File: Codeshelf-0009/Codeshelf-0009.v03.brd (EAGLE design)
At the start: 55.8 x 40.9 mm, 28 parts, among them J1 CONTACT-SPRING-S7071-42R, J2 CONTACT-SPRING-S7071-42R, J3 CONTACT-SPRING-S7071-42R, J4 CONTACT-SPRING-S7071-42R, U1 MC9S08QG-DT, U2 LED5060A, U3 RS485SOIC, U4 CAT9552

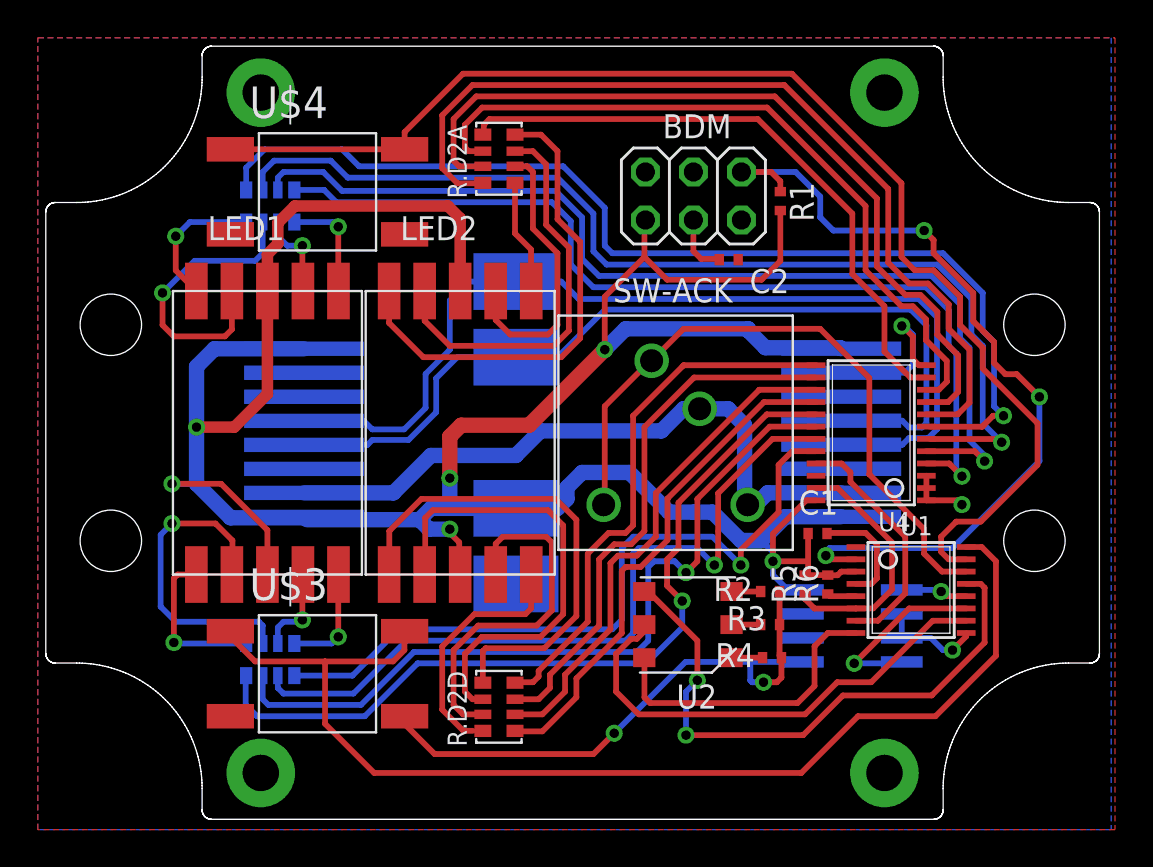
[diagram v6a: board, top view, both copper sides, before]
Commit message: New PosCon CAD model + routing
Added latest CAD model (sent to Marc) and did a little bit of routing.
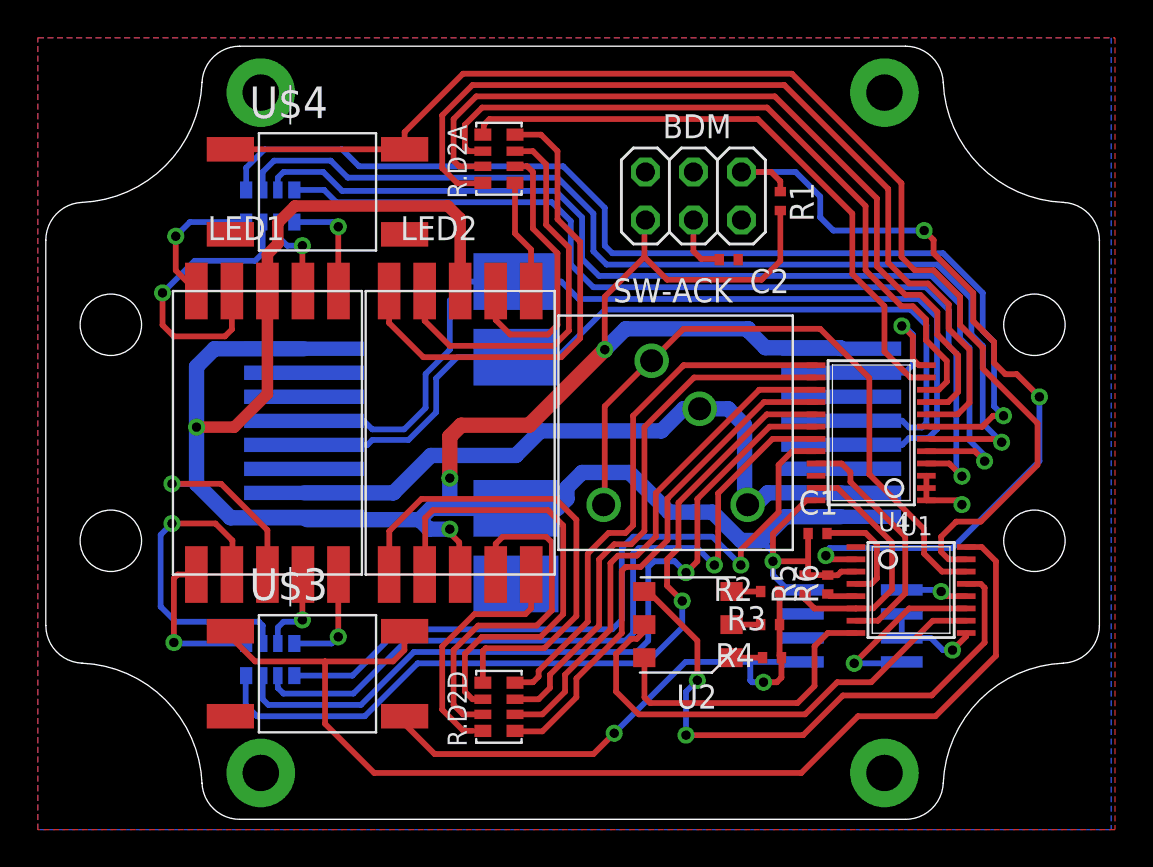
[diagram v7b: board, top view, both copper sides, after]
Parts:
- turned J2 to 270 degrees
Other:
- outline, holes or cut-outs redrawn

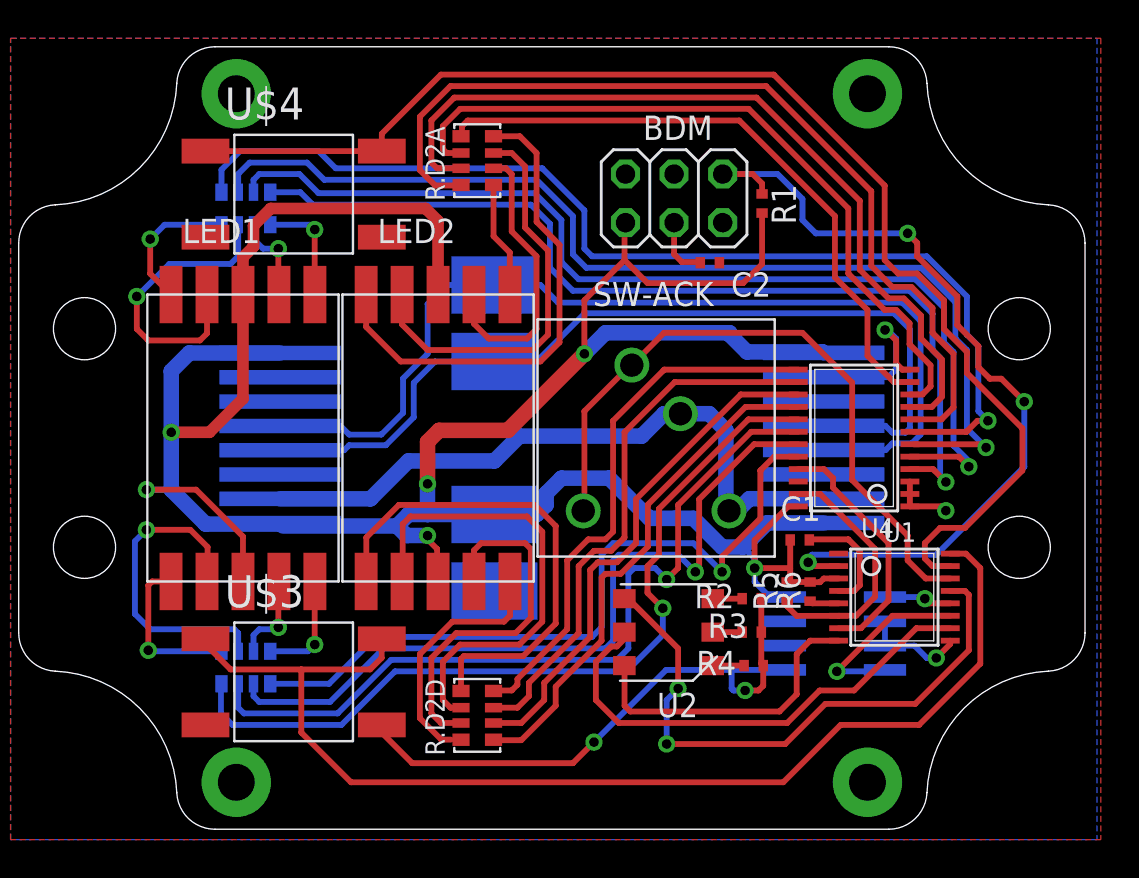
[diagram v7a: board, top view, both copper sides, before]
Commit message: New PosCon finished routing
Added RJ45 programming and awaiting new LED test.
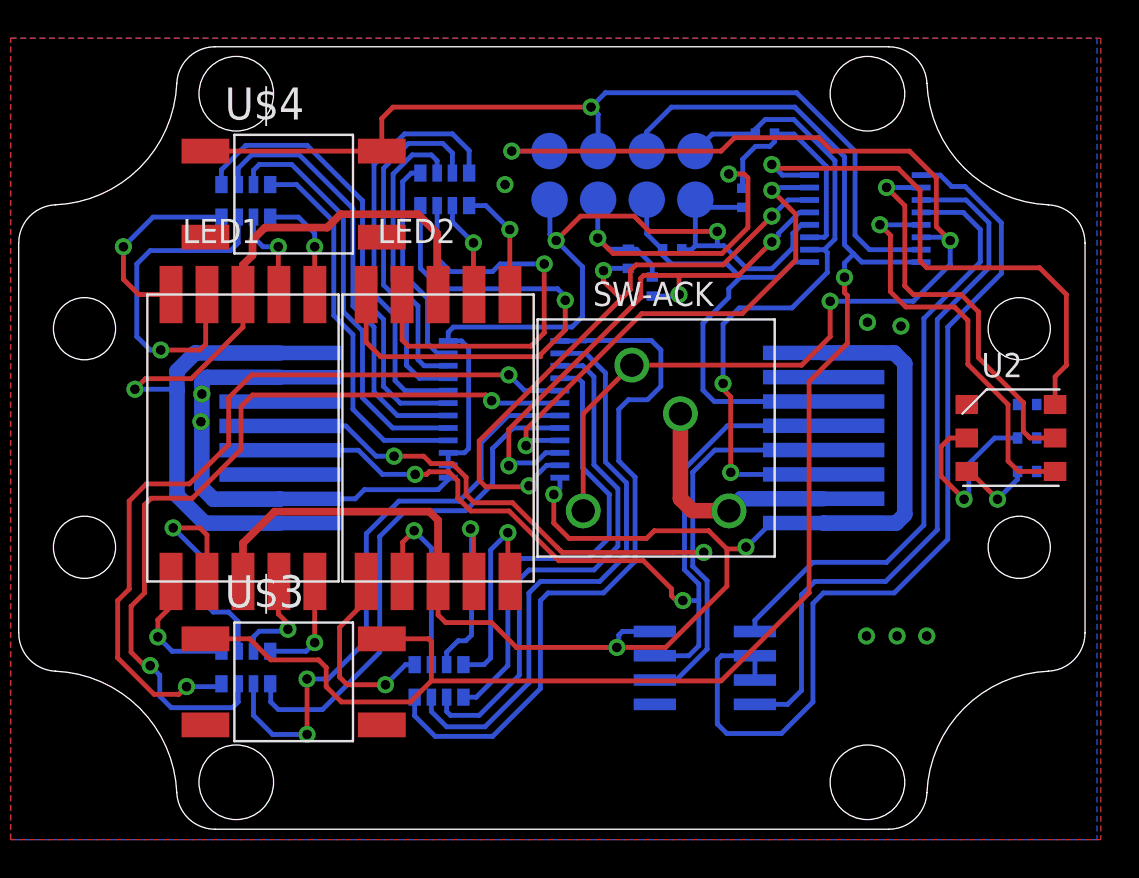
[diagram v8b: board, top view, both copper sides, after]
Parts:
- removed J1, J2, J3, J4: CONTACT-SPRING-S7071-42R, GW-devices:CONTACT-SPRING-S1761
- BDM: value HEADER-3X2 -> TP2X4SMD; device GW-devices:HEADER-3X2 -> GW-devices:SMD4X2
- moved U2 20.6 mm to (24.0, 0.00), turned to 0 degrees
- moved U1 19.8 mm to (16.4, 11.5), flipped to the bottom, turned to 90 degrees
- moved R4 19.8 mm to (24.9, 1.75), flipped to the bottom, turned to 180 degrees
- moved R5 19.3 mm to (4.00, 9.37), flipped to the bottom
- moved U4 18.4 mm to (-2.50, 1.50), flipped to the bottom
- moved C1 18.1 mm to (9.98, 12.6), flipped to the bottom, turned to 270 degrees
- moved R6 18.0 mm to (5.25, 7.92), flipped to the bottom
- moved R3 17.6 mm to (24.9, 0.00), flipped to the bottom, turned to 180 degrees
- moved R2 15.9 mm to (24.9, -1.75), flipped to the bottom, turned to 180 degrees
- moved U3 7.03 mm to (8.00, -12.0)
- moved BDM 3.84 mm to (7.50, 15.0), flipped to the bottom, turned to 0 degrees
- moved R1 3.63 mm to (11.1, 15.9), flipped to the bottom, turned to 180 degrees
- moved R.D2D 2.69 mm to (-5.90, -12.7), flipped to the bottom, turned to 0 degrees
- moved R.D2A 2.27 mm to (-5.60, 13.0), flipped to the bottom, turned to 0 degrees
- moved C2 2.08 mm to (6.29, 9.84), flipped to the bottom, turned to 0 degrees
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- renumbered U$2 to U$2-PROG
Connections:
- net +3V3: now also BDM.P$6; no longer BDM.6, J1.P1
- net 485_N: no longer J2.P1
- net 485_P: no longer J3.P1
- net GND: now also BDM.P$2, BDM.P$8; no longer BDM.2, J4.P1
- net N$23: now also BDM.P$4, U$1.P$3; no longer BDM.4
- net N$42: now also BDM.P$7
- net N$43: now also BDM.P$5
- net N$45: now also BDM.P$3
- net N$9: now also BDM.P$1, U$1.P$6; no longer BDM.1
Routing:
- net N$19: track 5.43 -> 49.1 mm, vias 1 -> 0
- net N$13: track 55.3 -> 22.7 mm, vias 1 -> 0
- net N$12: track 55.9 -> 23.8 mm, vias 1 -> 0
- net N$14: track 53.2 -> 21.7 mm, vias 1 -> 0
- net N$15: track 49.9 -> 20.0 mm, vias 1 -> 0
- net RX: track 3.55 -> 31.6 mm, vias 1 -> 0
- net TX: track 9.68 -> 37.4 mm, vias 1 -> 0
- net SLC: track 1.54 -> 28.4 mm, vias 0 -> 3
- net N$11: track 48.0 -> 21.9 mm
- net N$42: track 35.1 -> 61.1 mm, vias 0 -> 3
- net N$10: track 43.4 -> 18.7 mm
- net N$8: track 38.7 -> 15.4 mm
- net N$23: track 3.21 -> 25.0 mm
- net N$2: track 33.0 -> 11.4 mm
- net N$45: track 60.6 -> 81.3 mm, vias 0 -> 1
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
